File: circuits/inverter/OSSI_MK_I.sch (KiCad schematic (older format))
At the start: 0 parts

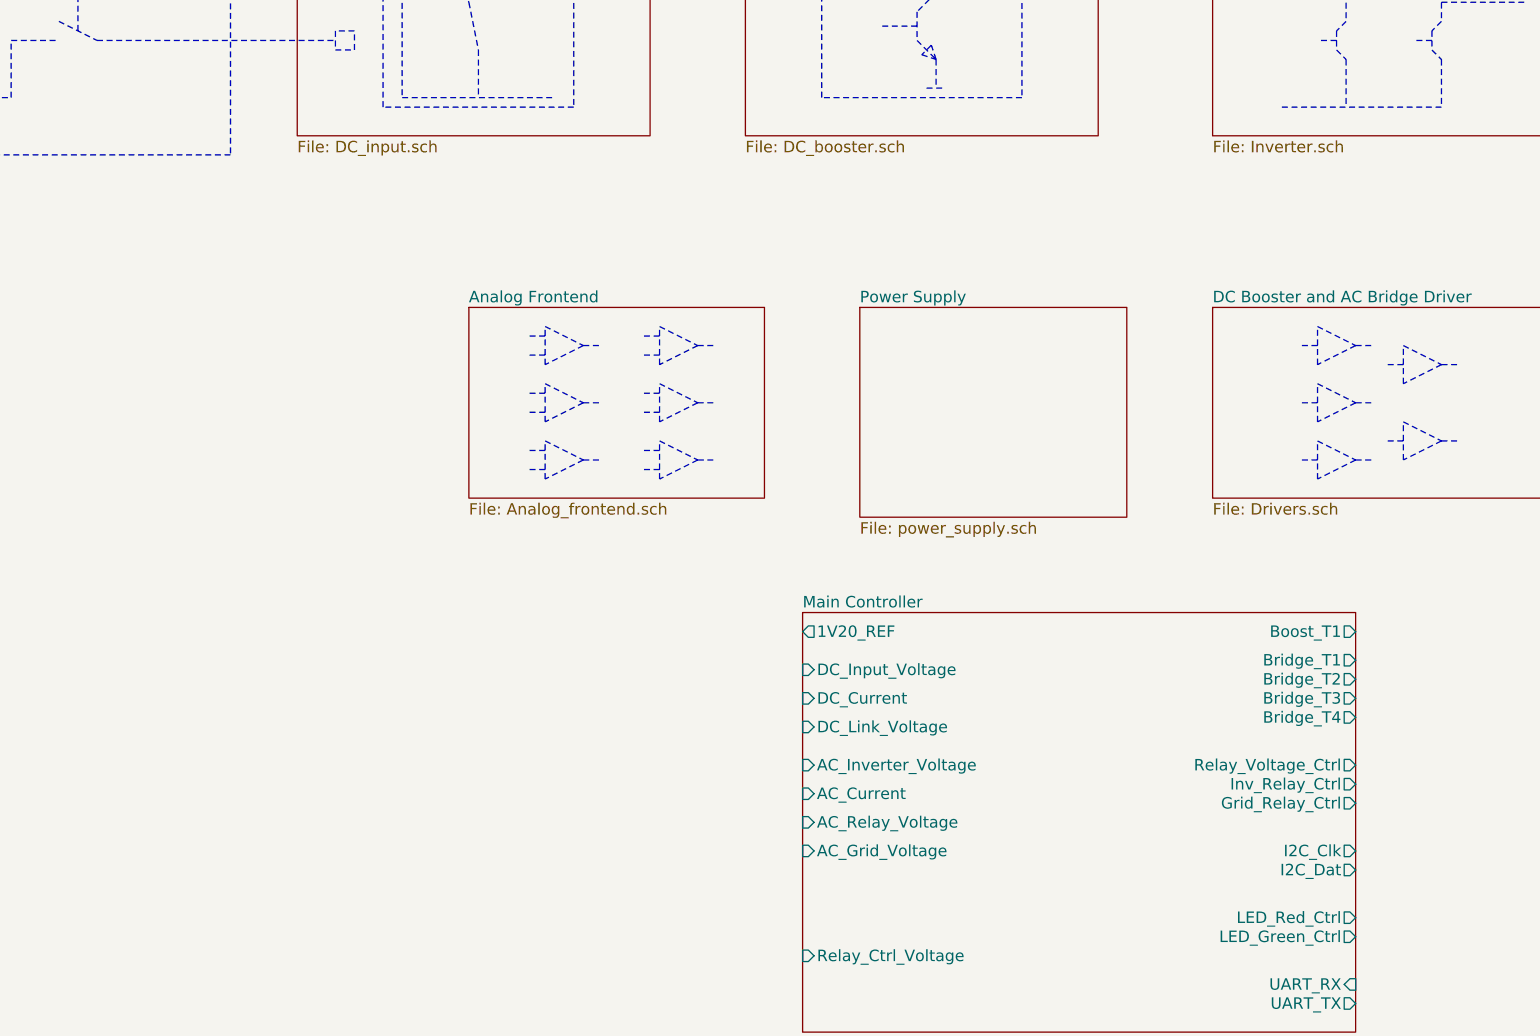
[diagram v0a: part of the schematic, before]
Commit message: Add analog frontend, add needed libraries
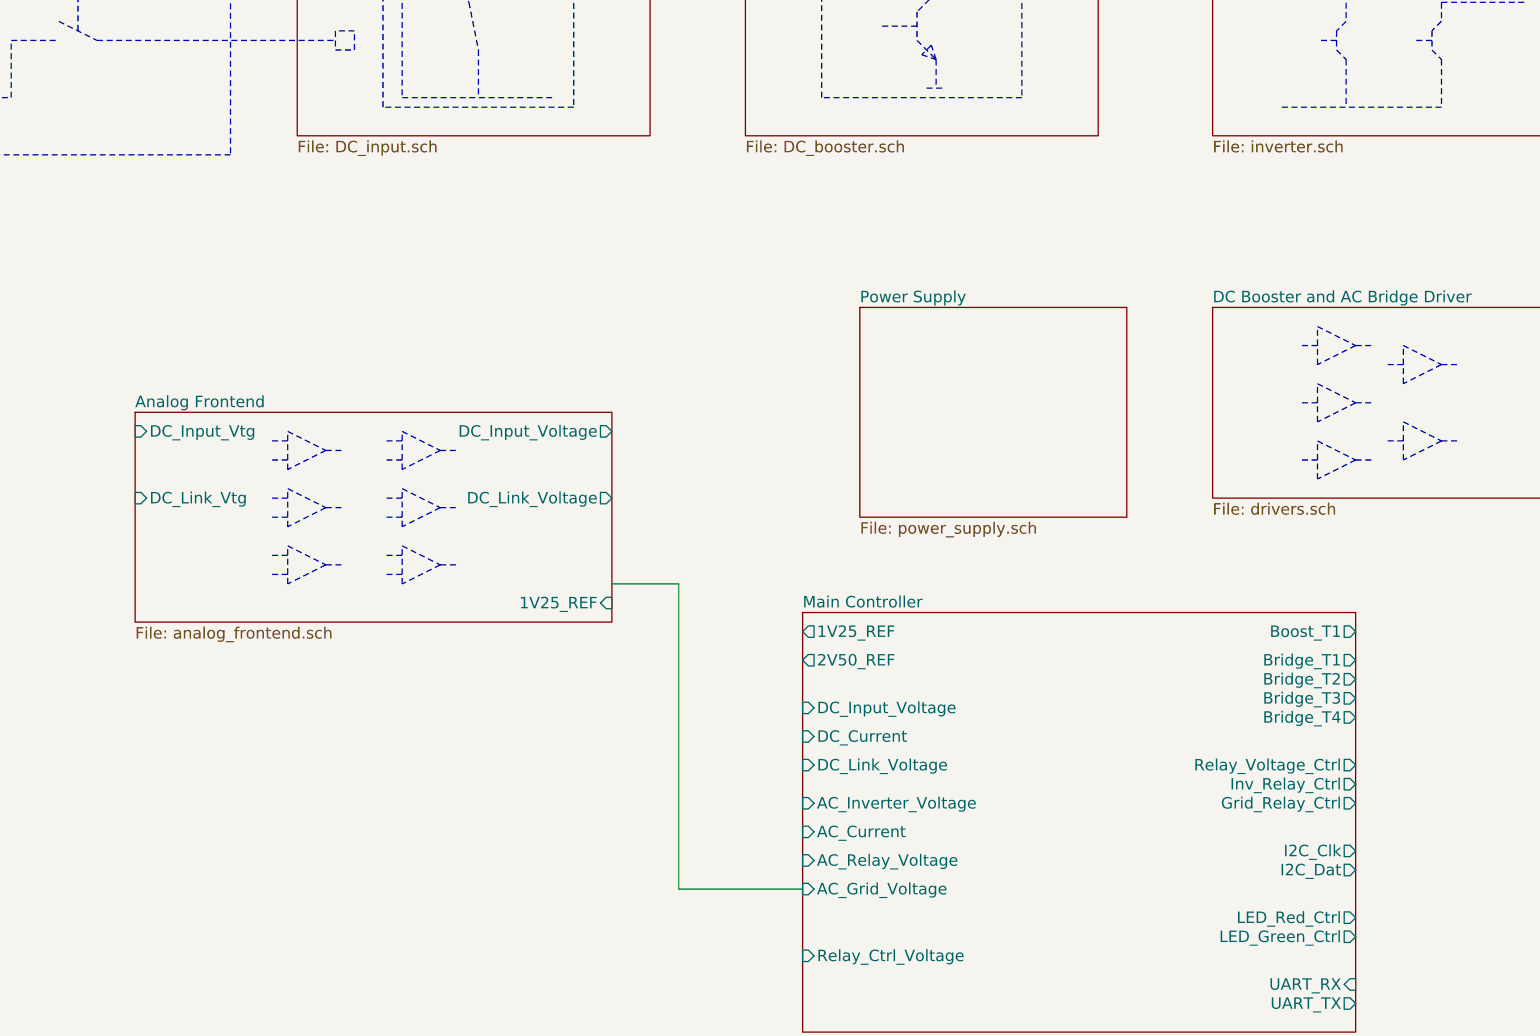
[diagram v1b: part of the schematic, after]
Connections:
- wire segments 0 -> 3
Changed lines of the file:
@@
 LIBS:OSSI_standard_components
 LIBS:connectors
+LIBS:lm4030
+LIBS:power
 LIBS:OSSI_MK_I-cache
 EELAYER 25 0
@@
 U 56D9C185
 F0 "Inverter Bridge" 60
-F1 "Inverter.sch" 60
+F1 "inverter.sch" 60
 $EndSheet
 $Sheet
@@
 U 56D9D1EC
 F0 "DC Booster and AC Bridge Driver " 60
-F1 "Drivers.sch" 60
-$EndSheet
-$Sheet
-S 3550 3600 1550 1000
+F1 "drivers.sch" 60
+$EndSheet
+$Sheet
+S 1800 4150 2500 1100
 U 56D9D375
 F0 "Analog Frontend" 60
-F1 "Analog_frontend.sch" 60
-$EndSheet
-Wire Notes Line
-	3950 3700 4150 3800
-Wire Notes Line
-	4150 3800 3950 3900
-Wire Notes Line
-	3950 3900 3950 3700
-Wire Notes Line
-	3950 3750 3850 3750
-Wire Notes Line
-	3950 3850 3850 3850
-Wire Notes Line
-	4150 3800 4250 3800
-Wire Notes Line
-	3950 4000 4150 4100
-Wire Notes Line
-	4150 4100 3950 4200
-Wire Notes Line
-	3950 4200 3950 4000
-Wire Notes Line
-	3950 4050 3850 4050
-Wire Notes Line
-	3950 4150 3850 4150
-Wire Notes Line
-	4150 4100 4250 4100
-Wire Notes Line
-	3950 4300 4150 4400
-Wire Notes Line
-	4150 4400 3950 4500
-Wire Notes Line
-	3950 4500 3950 4300
-Wire Notes Line
-	3950 4350 3850 4350
-Wire Notes Line
-	3950 4450 3850 4450
-Wire Notes Line
-	4150 4400 4250 4400
-Wire Notes Line
-	4550 3700 4750 3800
-Wire Notes Line
-	4750 3800 4550 3900
-Wire Notes Line
-	4550 3900 4550 3700
-Wire Notes Line
-	4550 3750 4450 3750
-Wire Notes Line
-	4550 3850 4450 3850
-Wire Notes Line
-	4750 3800 4850 3800
-Wire Notes Line
-	4550 4000 4750 4100
-Wire Notes Line
-	4750 4100 4550 4200
-Wire Notes Line
-	4550 4200 4550 4000
-Wire Notes Line
-	4550 4050 4450 4050
-Wire Notes Line
-	4550 4150 4450 4150
-Wire Notes Line
-	4750 4100 4850 4100
-Wire Notes Line
-	4550 4300 4750 4400
-Wire Notes Line
-	4750 4400 4550 4500
-Wire Notes Line
-	4550 4500 4550 4300
-Wire Notes Line
-	4550 4350 4450 4350
-Wire Notes Line
-	4550 4450 4450 4450
-Wire Notes Line
-	4750 4400 4850 4400
+F1 "analog_frontend.sch" 60
+F2 "DC_Input_Voltage" O R 4300 4250 60
+F3 "DC_Input_Vtg" I L 1800 4250 60
+F4 "DC_Link_Voltage" O R 4300 4600 60
+F5 "DC_Link_Vtg" I L 1800 4600 60
+F6 "1V25_REF" I R 4300 5150 60
+$EndSheet
+Wire Notes Line
+	2600 4250 2800 4350
+Wire Notes Line
+	2800 4350 2600 4450
+Wire Notes Line
+	2600 4450 2600 4250
+Wire Notes Line
+	2600 4300 2500 4300
+Wire Notes Line
+	2600 4400 2500 4400
+Wire Notes Line
+	2800 4350 2900 4350
+Wire Notes Line
+	2600 4550 2800 4650
+Wire Notes Line
+	2800 4650 2600 4750
+Wire Notes Line
+	2600 4750 2600 4550
+Wire Notes Line
+	2600 4600 2500 4600
+Wire Notes Line
+	2600 4700 2500 4700
+Wire Notes Line
+	2800 4650 2900 4650
+Wire Notes Line
+	2600 4850 2800 4950
+Wire Notes Line
+	2800 4950 2600 5050
+Wire Notes Line
+	2600 5050 2600 4850
+Wire Notes Line
+	2600 4900 2500 4900
+Wire Notes Line
+	2600 5000 2500 5000
+Wire Notes Line
+	2800 4950 2900 4950
+Wire Notes Line
+	3200 4250 3400 4350
+Wire Notes Line
+	3400 4350 3200 4450
+Wire Notes Line
+	3200 4450 3200 4250
+Wire Notes Line
+	3200 4300 3100 4300
+Wire Notes Line
+	3200 4400 3100 4400
+Wire Notes Line
+	3400 4350 3500 4350
+Wire Notes Line
+	3200 4550 3400 4650
+Wire Notes Line
+	3400 4650 3200 4750
+Wire Notes Line
+	3200 4750 3200 4550
+Wire Notes Line
+	3200 4600 3100 4600
+Wire Notes Line
+	3200 4700 3100 4700
+Wire Notes Line
+	3400 4650 3500 4650
+Wire Notes Line
+	3200 4850 3400 4950
+Wire Notes Line
+	3400 4950 3200 5050
+Wire Notes Line
+	3200 5050 3200 4850
+Wire Notes Line
+	3200 4900 3100 4900
+Wire Notes Line
+	3200 5000 3100 5000
+Wire Notes Line
+	3400 4950 3500 4950
 Wire Notes Line
 	8000 3700 8200 3800
@@
 F0 "Main Controller" 60
 F1 "main_controller.sch" 60
-F2 "1V20_REF" O L 5300 5300 60
-F3 "DC_Link_Voltage" I L 5300 5800 60
-F4 "AC_Grid_Voltage" I L 5300 6450 60
-F5 "AC_Current" I L 5300 6150 60
-F6 "AC_Relay_Voltage" I L 5300 6300 60
-F7 "DC_Input_Voltage" I L 5300 5500 60
-F8 "DC_Current" I L 5300 5650 60
-F9 "AC_Inverter_Voltage" I L 5300 6000 60
+F2 "1V25_REF" O L 5300 5300 60
+F3 "DC_Link_Voltage" I L 5300 6000 60
+F4 "AC_Grid_Voltage" I L 5300 6650 60
+F5 "AC_Current" I L 5300 6350 60
+F6 "AC_Relay_Voltage" I L 5300 6500 60
+F7 "DC_Input_Voltage" I L 5300 5700 60
+F8 "DC_Current" I L 5300 5850 60
+F9 "AC_Inverter_Voltage" I L 5300 6200 60
 F10 "Relay_Ctrl_Voltage" I L 5300 7000 60
 F11 "UART_RX" I R 8200 7150 60
@@
 F23 "Inv_Relay_Ctrl" O R 8200 6100 60
 F24 "Grid_Relay_Ctrl" O R 8200 6200 60
-$EndSheet
+F25 "2V50_REF" O L 5300 5450 60
+$EndSheet
+Wire Wire Line
+	5300 6650 4650 6650
+Wire Wire Line
+	4650 6650 4650 5050
+Wire Wire Line
+	4650 5050 4300 5050
 $EndSCHEMATC

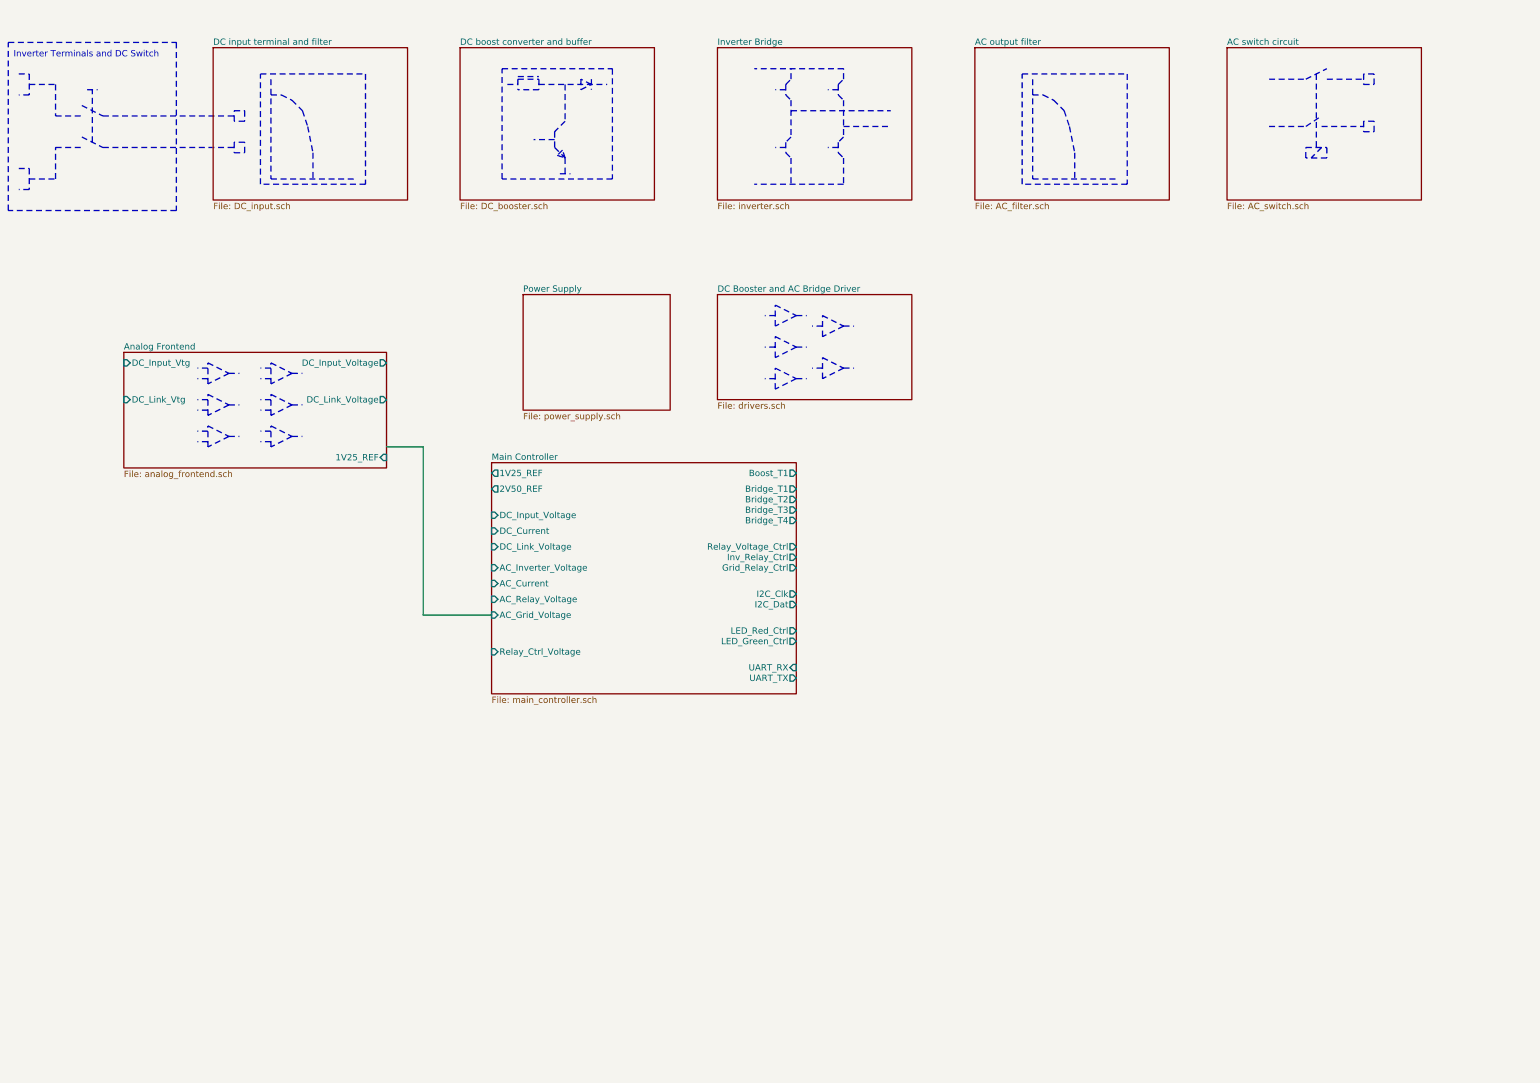
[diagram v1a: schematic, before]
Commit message: Add more circuitry, add library content
AC current measurement
AC filter
AC switch
DC booster
DC input
Analog frontend
drivers
inverter
main controller
power supply

new components for:
standard library (e.g. relay)
AC current sensor acs722
voltage regulator LM317L

Footprints for:
AC relay
TO-220
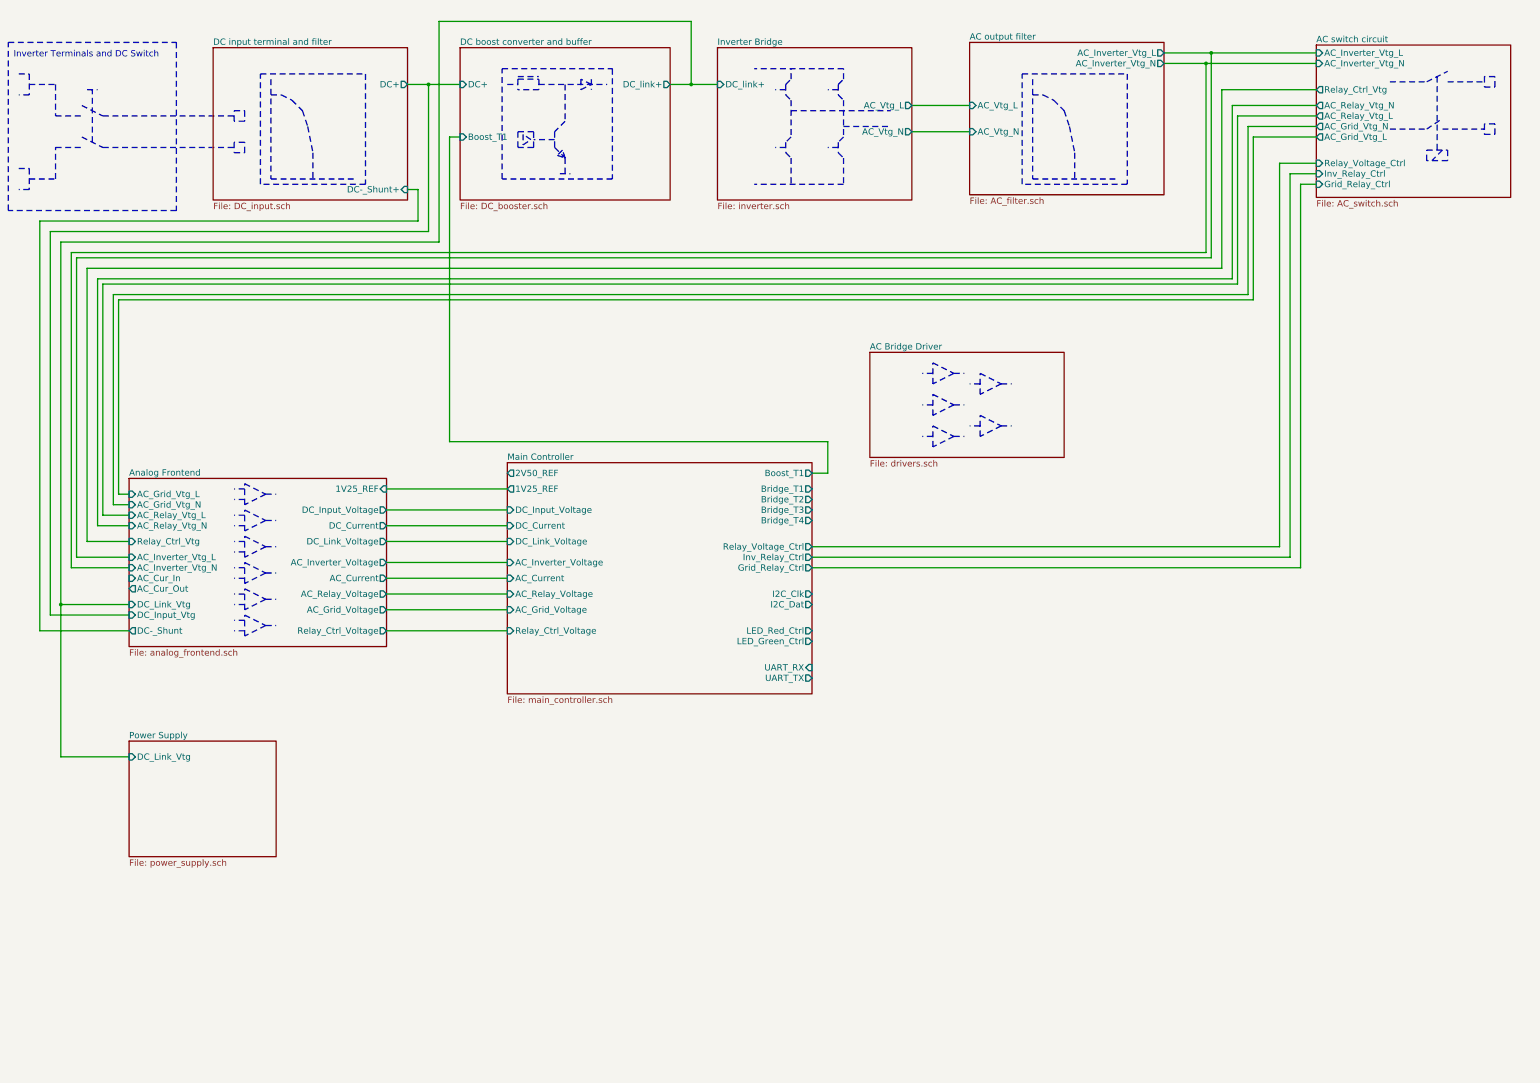
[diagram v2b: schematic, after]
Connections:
- wire segments 3 -> 78
